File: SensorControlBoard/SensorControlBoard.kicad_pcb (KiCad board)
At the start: 2 copper layers, 79 parts, among them J1 Micro_SD_Card, J10 Conn_01x05_Pin, J11 USB_C_Receptacle_USB2.0, J2 Conn_01x02_Pin, J3 Conn_02x10_Odd_Even, J4 Conn_01x10_Pin, J5 Conn_01x10_Pin, J6 Conn_01x02_Pin, J7 Conn_01x02_Pin, J8 Conn_01x02_Pin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

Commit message: Initial Routing finished
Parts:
- removed J3: Conn_02x10_Odd_Even, Connector_PinHeader_1.00mm:PinHeader_2x10_P1.00mm_Vertical
- added GPIO1: TestPoint, TestPoint:TestPoint_Pad_1.0x1.0mm, F.Cu at (91.2, 46.5)
- added GPIO10: TestPoint, TestPoint:TestPoint_Pad_1.0x1.0mm, F.Cu at (101.5, 61.6)
- added GPIO2: TestPoint, TestPoint:TestPoint_Pad_1.0x1.0mm, F.Cu at (107.8, 62.6)
- added GPIO3: TestPoint, TestPoint:TestPoint_Pad_1.0x1.0mm, F.Cu at (110.4, 57.7)
- added GPIO4: TestPoint, TestPoint:TestPoint_Pad_1.0x1.0mm, F.Cu at (112.5, 57.7)
- added GPIO5: TestPoint, TestPoint:TestPoint_Pad_1.0x1.0mm, F.Cu at (114.6, 56.3)
- added H1: MountingHole, MountingHole:MountingHole_2.2mm_M2, F.Cu at (121.5, 29.2)
- added H2: MountingHole, MountingHole:MountingHole_2.2mm_M2, F.Cu at (73.7, 29.2)
- added H3: MountingHole, MountingHole:MountingHole_2.2mm_M2, F.Cu at (73.7, 72.4)
- added H4: MountingHole, MountingHole:MountingHole_2.2mm_M2, F.Cu at (121.5, 72.4)
- moved J5 53.2 mm to (108.1, 26.5), turned to -90 degrees
- moved SW1 39.1 mm to (80.4, 33.0), turned to 90 degrees
- moved R2 31.4 mm to (77.0, 36.3), turned to 90 degrees
- moved J4 29.3 mm to (86.7, 27.6), turned to 90 degrees
- moved C8 15.2 mm to (110.0, 48.3), turned to 0 degrees
- moved R8 8.58 mm to (85.3, 73.3), turned to -90 degrees
- moved R9 5.48 mm to (87.9, 74.3), turned to -90 degrees
- moved C17 4.23 mm to (82.1, 42.8)
- moved R14 4.23 mm to (83.9, 42.8)
- moved U5 4.23 mm to (85.4, 47.6)
- moved J11 3.82 mm to (124.4, 52.0)
- moved R15 3.66 mm to (117.1, 54.0)
- moved R16 3.62 mm to (117.1, 50.3)
- moved R13 3.53 mm to (90.0, 42.7)
- moved R12 3.28 mm to (88.4, 42.7)
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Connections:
- D3 pad 1: GPIO_4 -> GPIO_7
- J1 pad 2: GPIO_5 -> GPIO_9
- J4 pad 1: /uController/GPIO_11 -> /uController/BOOT0
- J4 pad 10: SPI1_SCK -> /uController/ADC1_0
- J4 pad 2: /uController/GPIO_12 -> +3.3V
- J4 pad 3: /uController/GPIO_13 -> GND
- J4 pad 4: /uController/GPIO_14 -> +3.3V
- J4 pad 5: /uController/ADC1_0 -> GND
- J4 pad 6: /uController/ADC1_7 -> /uController/ADC2_6
- J4 pad 7: /uController/ADC1_8 -> /uController/ADC1_7
- J4 pad 8: /uController/ADC2_5 -> /uController/ADC1_8
- J4 pad 9: /uController/ADC2_6 -> /uController/ADC2_5
- J5 pad 10: /uController/BOOT0 -> /uController/UART1_RX
- J5 pad 3: /uController/UART1_TX -> SPI1_SCK
- J5 pad 4: /uController/UART1_RX -> unconnected-(J5-Pin_4-Pad4)
- J5 pad 9: /uController/NRST -> /uController/UART1_TX
- MT1 pad 4: GPIO_7 -> GPIO_14
- MT1 pad 9: GPIO_8 -> GPIO_13
- R10 pad 2: GPIO_2 -> GPIO_6
- R19 pad 2: GPIO_5 -> GPIO_9
- R20 pad 1: GPIO_6 -> GPIO_12
- R21 pad 2: GPIO_6 -> GPIO_12
- R24 pad 2: GPIO_1 -> GPIO_11
- R6 pad 2: GPIO_4 -> GPIO_7
- R7 pad 2: GPIO_2 -> GPIO_6
- U1 pad 11: /uController/GPIO_7 -> GPIO_7
- U1 pad 12: /uController/GPIO_8 -> GPIO_8
- U1 pad 13: /uController/GPIO_9 -> GPIO_9
- U1 pad 14: /uController/GPIO_10 -> GPIO_10
- U1 pad 25: /uController/GPIO_3 -> GPIO_3
- U1 pad 26: /uController/GPIO_4 -> GPIO_4
- U1 pad 27: /uController/GPIO_5 -> GPIO_5
- U1 pad 28: /uController/GPIO_6 -> GPIO_6
- U1 pad 29: /uController/GPIO_11 -> GPIO_11
- U1 pad 30: /uController/GPIO_12 -> GPIO_12
- U1 pad 31: /uController/GPIO_13 -> GPIO_13
- U1 pad 38: /uController/GPIO_14 -> GPIO_14
- U13 pad 5: GPIO_6 -> GPIO_12
- U3 pad 5: GPIO_4 -> GPIO_7
- U4 pad 4: GPIO_1 -> GPIO_11
- U4 pad 8: GPIO_2 -> GPIO_6
- U5 pad 30: GPIO_3 -> GPIO_8
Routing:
- net +3.3V: track 0.00 -> 316.0 mm, vias 0 -> 2
- net /uController/I2C2_SCL: track 0.00 -> 134.1 mm, vias 0 -> 2
- net /uController/I2C2_SDA: track 0.00 -> 128.9 mm, vias 0 -> 2
- net /uController/ADC1_7: track 0.00 -> 126.9 mm, vias 0 -> 3
- net SPI1_SCK: track 0.00 -> 115.7 mm, vias 0 -> 4
- net SPI1_MOSI: track 0.00 -> 96.4 mm, vias 0 -> 3
- net GND: track 0.00 -> 90.3 mm, vias 0 -> 35
- net /uController/ADC2_6: track 0.00 -> 87.7 mm, vias 0 -> 3
- net SPI1_MISO: track 0.00 -> 87.2 mm, vias 0 -> 3
- net /uController/ADC1_8: track 0.00 -> 84.2 mm, vias 0 -> 3
- net /uController/ADC2_5: track 0.00 -> 82.0 mm, vias 0 -> 3
- net I2C1_SCL: track 0.00 -> 74.4 mm, vias 0 -> 3
- net /uController/BOOT0: track 0.00 -> 63.7 mm, vias 0 -> 2
- net I2C1_SDA: track 0.00 -> 61.6 mm, vias 0 -> 4
- net /uController/UART1_RX: track 0.00 -> 48.1 mm, vias 0 -> 1
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- added copper zone on F.Cu, net +3.3V
- added copper zone on B.Cu, net GND
- added copper zone on F.Cu, net GND
- added copper zone on F.Cu, net VBUS
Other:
- board outline added: 58.4 x 53.9 mm
- copper layers 2 -> 4

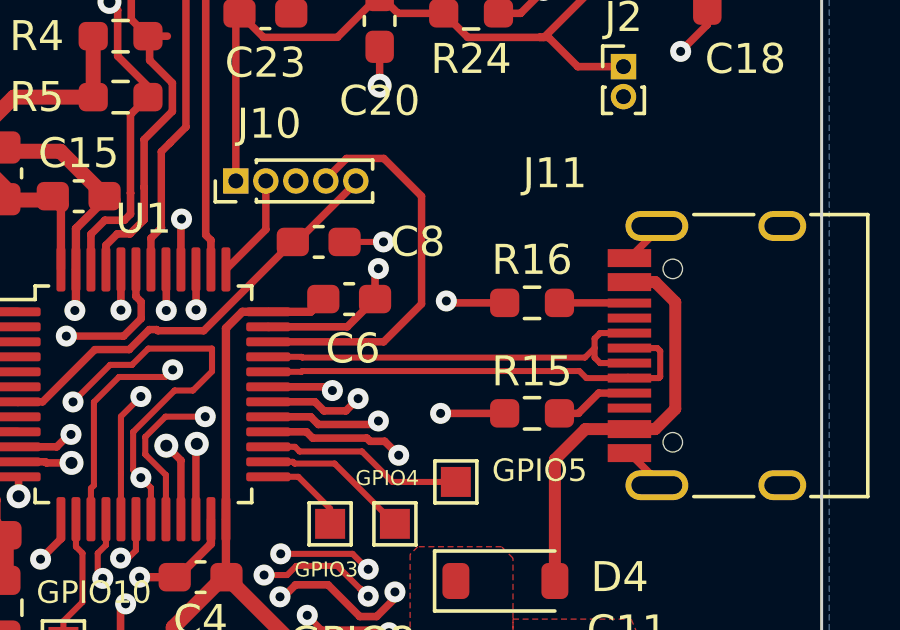
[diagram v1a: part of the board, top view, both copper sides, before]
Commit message: added TVS protection diodes
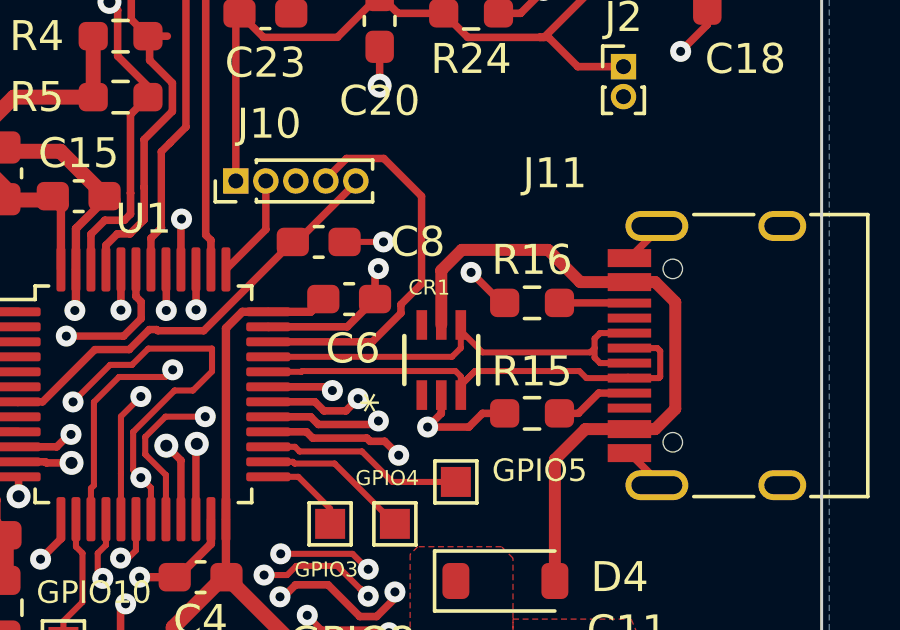
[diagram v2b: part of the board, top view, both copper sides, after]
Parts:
- added CR1: NUP4114UCLW1T2G, NUP4114:SC-88&slash_SC70-6&slash_SOT-363_419B-02_ONS_OSI-M, F.Cu at (114.1, 52.2)
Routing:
- net /uController/VBUS_USB: track 14.1 -> 22.9 mm
- net /uController/USB-: track 15.2 -> 16.7 mm
- net GND: track 90.3 -> 91.8 mm
- net /uController/USB+: track 14.1 -> 15.0 mm

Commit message: A0 PCB Commit
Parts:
- moved J5 1.02 mm to (108.1, 27.6)
- moved R2 0.51 mm to (76.5, 36.3)
- renumbered MT1 to U14
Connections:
- J4 pad 2: +3.3V -> GPIO_10
- J4 pad 3: GND -> GPIO_2
- J4 pad 4: +3.3V -> GPIO_3
- J5 pad 4: unconnected-(J5-Pin_4-Pad4) -> GND
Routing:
- net GPIO_3: track 3.01 -> 116.6 mm, vias 0 -> 1
- net GPIO_2: track 15.0 -> 126.3 mm, vias 2 -> 4
- net GPIO_10: track 4.45 -> 69.3 mm, vias 0 -> 2
- net +3.3V: track 316.0 -> 306.4 mm
- net GND: track 91.8 -> 98.5 mm, vias 35 -> 38
- net SPI1_MISO: track 87.2 -> 84.5 mm
- net /uController/PWR_LED_K: track 0.00 -> 2.02 mm
- net I2C1_SCL: track 74.4 -> 72.4 mm
- net /uController/UART1_TX: track 28.1 -> 26.4 mm
- net /uController/BOOT0: track 63.7 -> 65.1 mm
- net SPI1_MOSI: track 96.4 -> 95.2 mm
- net I2C1_SDA: track 61.6 -> 60.6 mm
- net GPIO_7: track 42.9 -> 41.9 mm, vias 3 -> 2
- net /uController/UART1_RX: track 48.1 -> 47.1 mm
- net /uController/ADC1_7: track 126.9 -> 127.8 mm
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- added copper zone on In1.Cu, net GND
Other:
- board text added: "0"
- board text added: "0 mils"
- board text added: "0.02"
- board text added: "0.1016 mm / 0.1016 mm"
- board text added: "0.3000 mm"
- board text added: "0.4 mils"
- board text added: "0.6 mils"
- board text added: "1"
- board text added: "1.38 mils"
- board text added: "1.6000 mm"
- board text added: "10"
- board text added: "1_0"
- board text added: "1_7"
- board text added: "1_8"
- board text added: "1_MISO"
- board text added: "1_MOSI"
- board text added: "1_RX"
- board text added: "1_SCK"
- board text added: "1_SCL"
- board text added: "1_SDA"
- board text added: "1_TX"
- board text added: "2"
- board text added: "2_5"
- board text added: "2_6"
- board text added: "2_SCL"
- board text added: "2_SDA"
- board text added: "3"
- board text added: "3.3"
- board text added: "3.91 mils"
- board text added: "4"
- board text added: "4.5"
- board text added: "49.8 mils"
- board text added: "58.4200 mm x 53.8540 mm"
- board text added: "ADC"
- board text added: "B.Cu"
- board text added: "B.Mask"
- board text added: "B.Paste"
- board text added: "B.Silkscreen"
- board text added: "BOARD CHARACTERISTICS"
- board text added: "BOOT0"
- board text added: "Board Thickness:"
- board text added: "Board overall dimensions:"
- board text added: "Bottom Silk Screen"
- board text added: "Bottom Solder Mask"
- board text added: "Bottom Solder Paste"
- board text added: "Castellated pads:"
- board text added: "Color"
- board text added: "Copper Finish:"
- board text added: "Copper Layer Count:"
- board text added: "Dielectric 1"
- board text added: "Dielectric 2"
- board text added: "Dielectric 3"
- board text added: "Edge card connectors:"
- board text added: "Epsilon R"
- board text added: "F.Cu"
- board text added: "F.Mask"
- board text added: "F.Paste"
- board text added: "F.Silkscreen"
- board text added: "FR4"
- board text added: "GND"
- board text added: "GPIO"
- board text added: "I2C"
- board text added: "Impedance Control:"
- board text added: "In1.Cu"
- board text added: "In2.Cu"
- board text added: "Layer Name"
- board text added: "Loss Tangent"
- board text added: "Material"
- board text added: "Min hole diameter:"
- board text added: "Min track/spacing:"
- board text added: "No"
- board text added: "None"
- board text added: "Not specified"
- board text added: "Plated Board Edge:"
- board text added: "SPI"
- board text added: "Thickness (mils)"
- board text added: "Top -> 6.16 L1 -> 5.41"
- board text added: "Top Silk Screen"
- board text added: "Top Solder Mask"
- board text added: "Top Solder Paste"
- board text added: "Type"
- board text added: "UART"
- board text added: "copper"
- board text added: "core"
- board text added: "prepreg"
